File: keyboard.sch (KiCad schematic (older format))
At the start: 16 parts

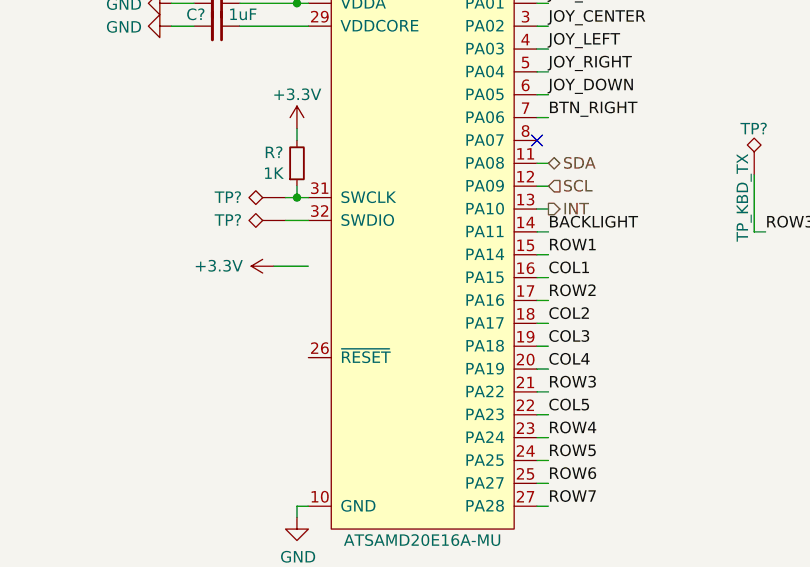
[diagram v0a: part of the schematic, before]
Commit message: Added display, and keyboard reset pin
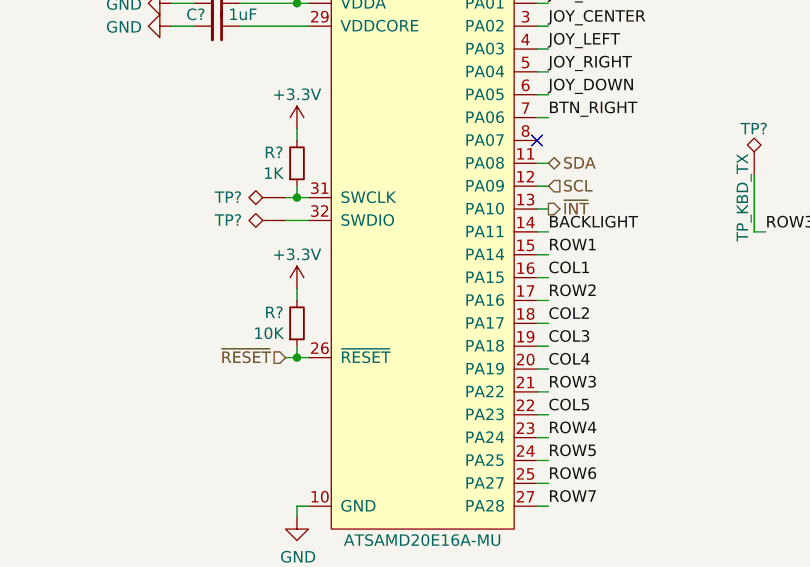
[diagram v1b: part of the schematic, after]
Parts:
- added R?: 10K, symbol Device:R_Small
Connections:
- net +3V3: now also R?.2
- net ~RESET~: now reaches U?.26 (~RESET~)
- net ~RESET~: now also R?.1
- net INT renamed ~INT~
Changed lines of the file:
@@
 $Descr A4 11693 8268
 encoding utf-8
-Sheet 2 2
+Sheet 2 3
 Title "Keyboard"
 Date ""
@@
 	8100 4700 8150 4700
 Wire Wire Line
-	7100 3650 6950 3650
-Wire Wire Line
 	7100 4700 7050 4700
 Wire Wire Line
@@
 $EndComp
 NoConn ~ 8100 3100
-$Comp
-L power:+3.3V #PWR?
-U 1 1 5C47BF0D
-P 6950 3650
-F 0 "#PWR?" H 6950 3500 50  0001 C CNN
-F 1 "+3.3V" V 6950 4000 50  0000 R CNN
-F 2 "" H 6950 3650 50  0001 C CNN
-F 3 "" H 6950 3650 50  0001 C CNN
-	1    6950 3650
-	0    -1   -1   0
-$EndComp
 $Comp
 L power:+3.3V #PWR?
@@
 BTN_RIGHT
 Text HLabel 8150 3400 2    50   Output ~ 0
-INT
+~INT~
 Text HLabel 8150 3300 2    50   Input ~ 0
 SCL
@@
 Text Label 9100 3500 0    50   ~ 0
 ROW3
+Wire Wire Line
+	7050 3750 7050 3800
+$Comp
+L power:+3.3V #PWR?
+U 1 1 5C522576
+P 7050 3750
+F 0 "#PWR?" H 7050 3600 50  0001 C CNN
+F 1 "+3.3V" H 7050 3900 50  0000 C CNN
+F 2 "" H 7050 3750 50  0001 C CNN
+F 3 "" H 7050 3750 50  0001 C CNN
+	1    7050 3750
+	1    0    0    -1
+$EndComp
+$Comp
+L Device:R_Small R?
+U 1 1 5C522580
+P 7050 3900
+F 0 "R?" H 6992 3854 50  0000 R CNN
+F 1 "10K" H 6992 3945 50  0000 R CNN
+F 2 "" H 7050 3900 50  0001 C CNN
+F 3 "~" H 7050 3900 50  0001 C CNN
+	1    7050 3900
+	1    0    0    1
+$EndComp
+Wire Wire Line
+	7050 4050 7050 4000
+Wire Wire Line
+	7000 4050 7050 4050
+Connection ~ 7050 4050
+Wire Wire Line
+	7050 4050 7100 4050
+Text HLabel 7000 4050 0    50   Input ~ 0
+~RESET~
 $EndSCHEMATC
